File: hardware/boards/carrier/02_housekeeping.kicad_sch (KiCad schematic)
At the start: 11 parts, among them SW1 SKSCLCE010, U1 STM32G031G6U6

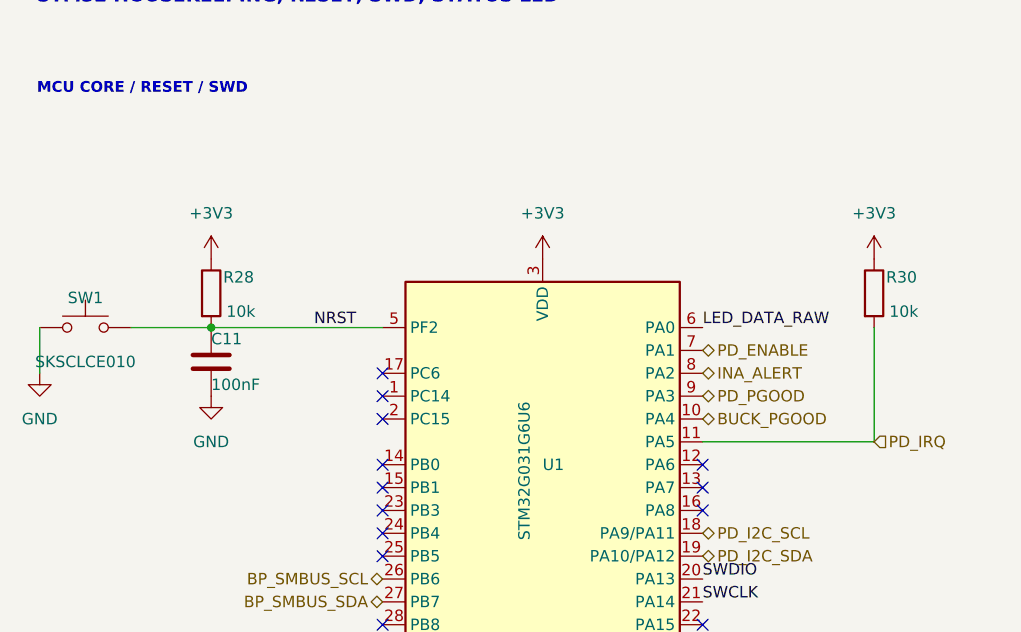
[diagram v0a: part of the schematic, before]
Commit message: hardware: move carrier button to GPIO
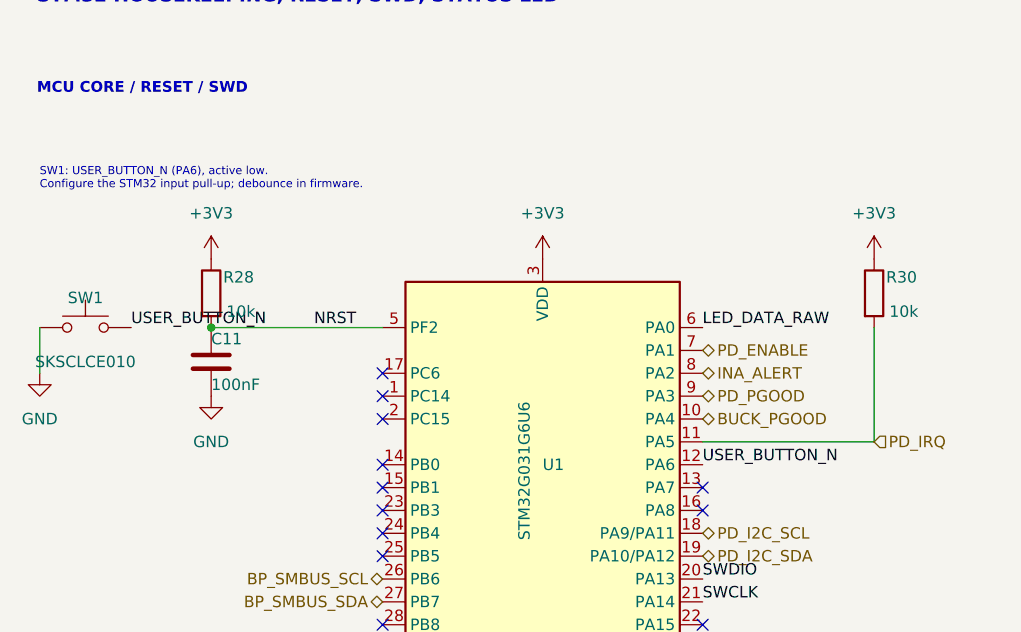
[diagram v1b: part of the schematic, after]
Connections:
- net NRST: no longer SW1.2
- net USER_BUTTON_N: now reaches U1.12 (PA6)
- net USER_BUTTON_N: now also SW1.2
- no-connect marks 14 -> 13
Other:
- note added: "SW1: USER_BUTTON_N (PA6), active low. Configure the STM32 input pull-up; debounce in firmware."
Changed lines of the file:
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@@
+		)
+	)
+	(text "SW1: USER_BUTTON_N (PA6), active low.\nConfigure the STM32 input pull-up; debounce in firmware."
+		(exclude_from_sim no)
+		(at 20.32 35.56 0)
+		(effects
+			(font
+				(size 0.9 0.9)
+			)
+			(justify left bottom)
 		)
 	)
@@
 		)
 	)
-	(wire
-		(pts
-			(xy 30.48 50.8) (xy 39.37 50.8)
-		)
-		(stroke
-			(width 0)
-			(type default)
-		)
-	)
 	(no_connect
 		(at 58.42 58.42)
-	)
-	(no_connect
-		(at 93.98 66.04)
 	)
 	(no_connect
@@
 		)
 	)
+	(label "USER_BUTTON_N"
+		(at 30.48 50.8 0)
+		(effects
+			(font
+				(size 1.27 1.27)
+			)
+			(justify left bottom)
+		)
+	)
+	(label "USER_BUTTON_N"
+		(at 93.98 66.04 0)
+		(effects
+			(font
+				(size 1.27 1.27)
+			)
+			(justify left bottom)
+		)
+	)

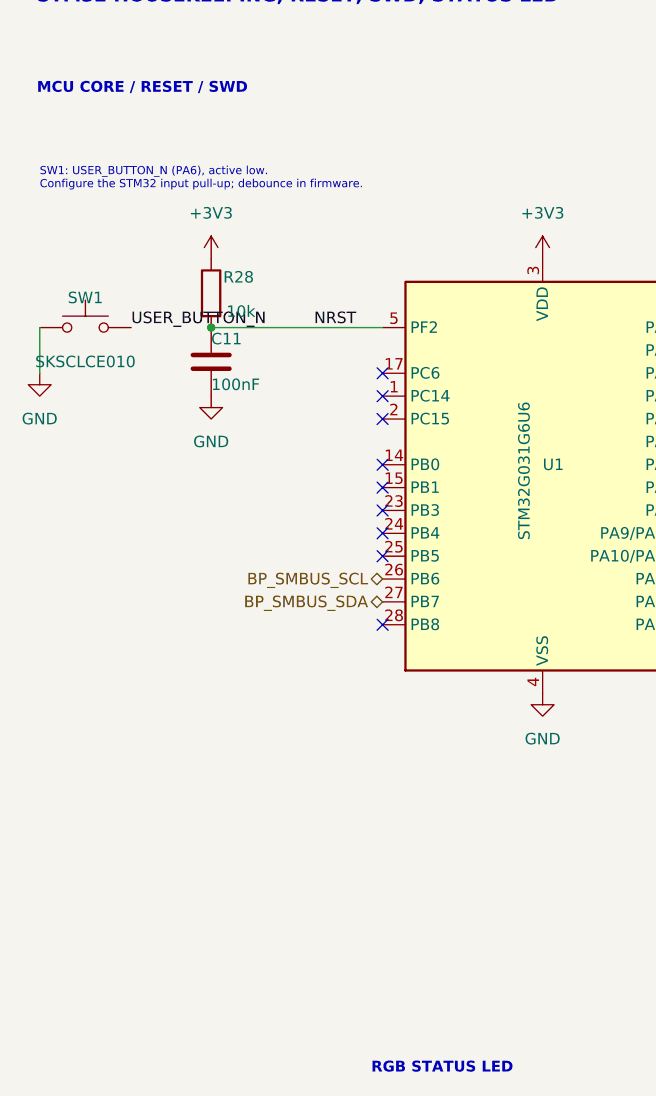
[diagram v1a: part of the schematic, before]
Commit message: hardware: add button debounce and ground stitching via
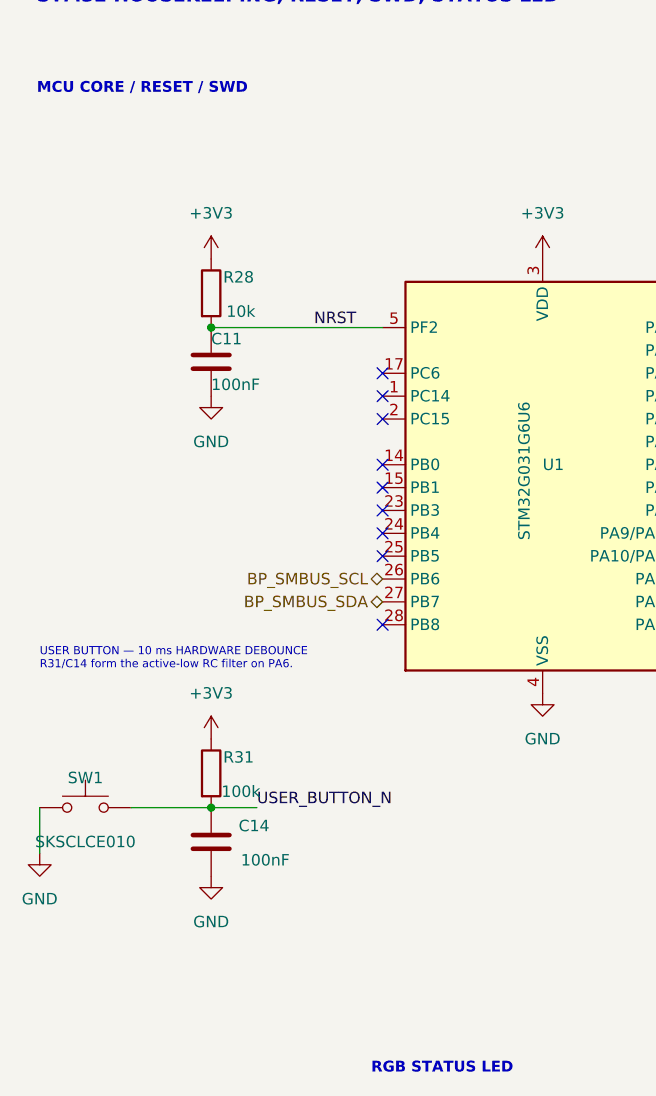
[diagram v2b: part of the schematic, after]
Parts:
- added C14: 100nF, Capacitor_SMD:C_0603_1608Metric, symbol Device:C
- added R31: 100k, Resistor_SMD:R_0603_1608Metric, symbol Device:R
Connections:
- net +3V3: now also R31.1
- net GND: now also C14.2
- net USER_BUTTON_N: now also C14.1, R31.2
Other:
- note added: "USER BUTTON — 10 ms HARDWARE DEBOUNCE R31/C14 form the active-low RC filter on PA6."
- note removed: "SW1: USER_BUTTON_N (PA6), active low. Configure the STM32 input pull-up; debounce in firmware."
- moved on the sheet: SW1

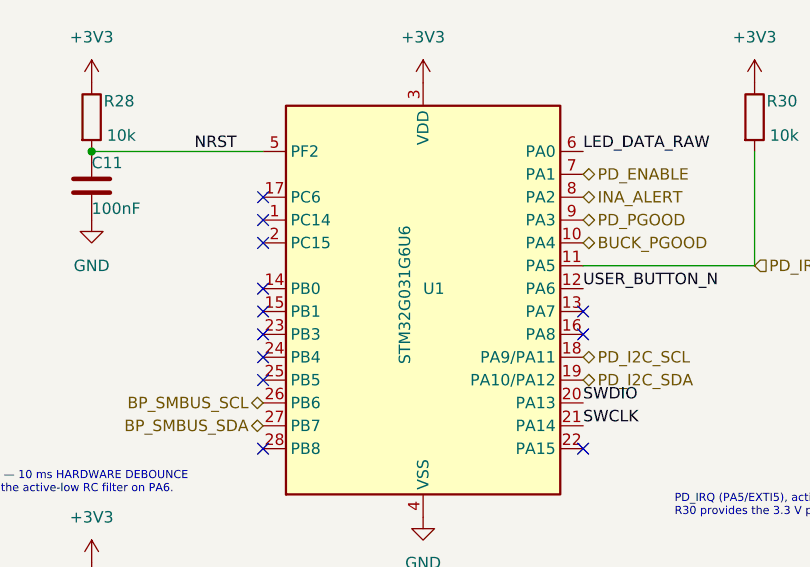
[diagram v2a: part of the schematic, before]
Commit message: Replace carrier MCU with STM32C092GCU7
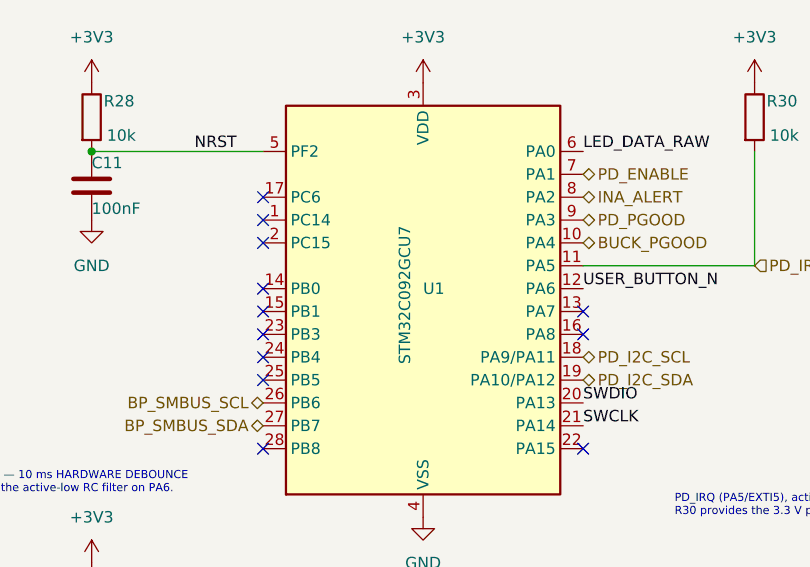
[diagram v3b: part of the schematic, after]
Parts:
- U1: value STM32G031G6U6 -> STM32C092GCU7; symbol MCU_ST_STM32G0:STM32G031G6Ux -> mini-rack-power:STM32C092GCUx; LCSC C432210 -> (none); MPN STM32G031G6U6 -> STM32C092GCU7
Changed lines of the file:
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@@
 	)
 	(symbol
-		(lib_id "MCU_ST_STM32G0:STM32G031G6Ux")
+		(lib_id "mini-rack-power:STM32C092GCUx")
 		(at 76.2 68.58 0)
 		(unit 1)
@@
 			)
 		)
-		(property "Value" "STM32G031G6U6"
+		(property "Value" "STM32C092GCU7"
 			(at 74.168 74.422 90)
 			(show_name no)
@@
 			)
 		)
-		(property "Datasheet" "https://www.st.com/resource/en/datasheet/stm32g031g6.pdf"
+		(property "Datasheet" "https://www.st.com/resource/en/datasheet/stm32c092gc.pdf"
 			(at 76.2 68.58 0)
 			(hide yes)
@@
 			)
 		)
-		(property "Description" "STMicroelectronics Arm Cortex-M0+ MCU, 32KB flash, 8KB RAM, 64 MHz, 1.7-3.6V, 26 GPIO, UFQFPN28"
+		(property "Description" "STMicroelectronics Arm Cortex-M0+ MCU, 256KB flash, 30KB RAM, 48 MHz, 2.0-3.6V, FDCAN, 26 GPIO, UFQFPN28"
 			(at 76.2 68.58 0)
 			(hide yes)
@@
 			)
 		)
-		(property "MPN" "STM32G031G6U6"
+		(property "MPN" "STM32C092GCU7"
 			(at 76.2 68.58 0)
 			(hide yes)
@@
 			)
 		)
-		(property "LCSC" "C432210"
+		(property "LCSC" ""
 			(at 76.2 68.58 0)
 			(hide yes)

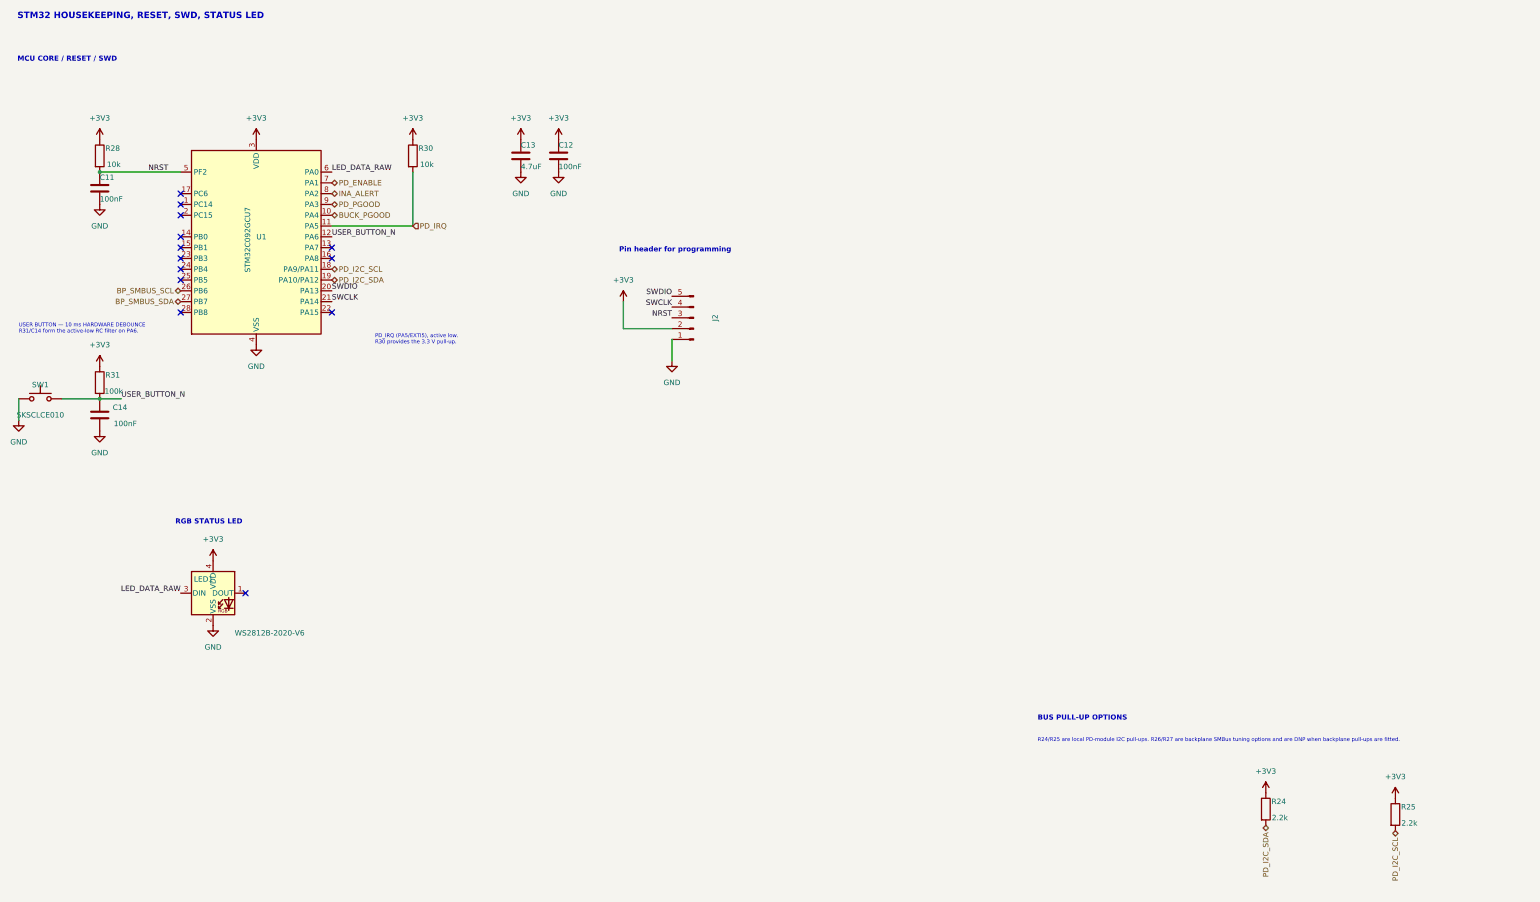
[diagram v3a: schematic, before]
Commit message: Replace carrier backplane SMBus with CAN-FD
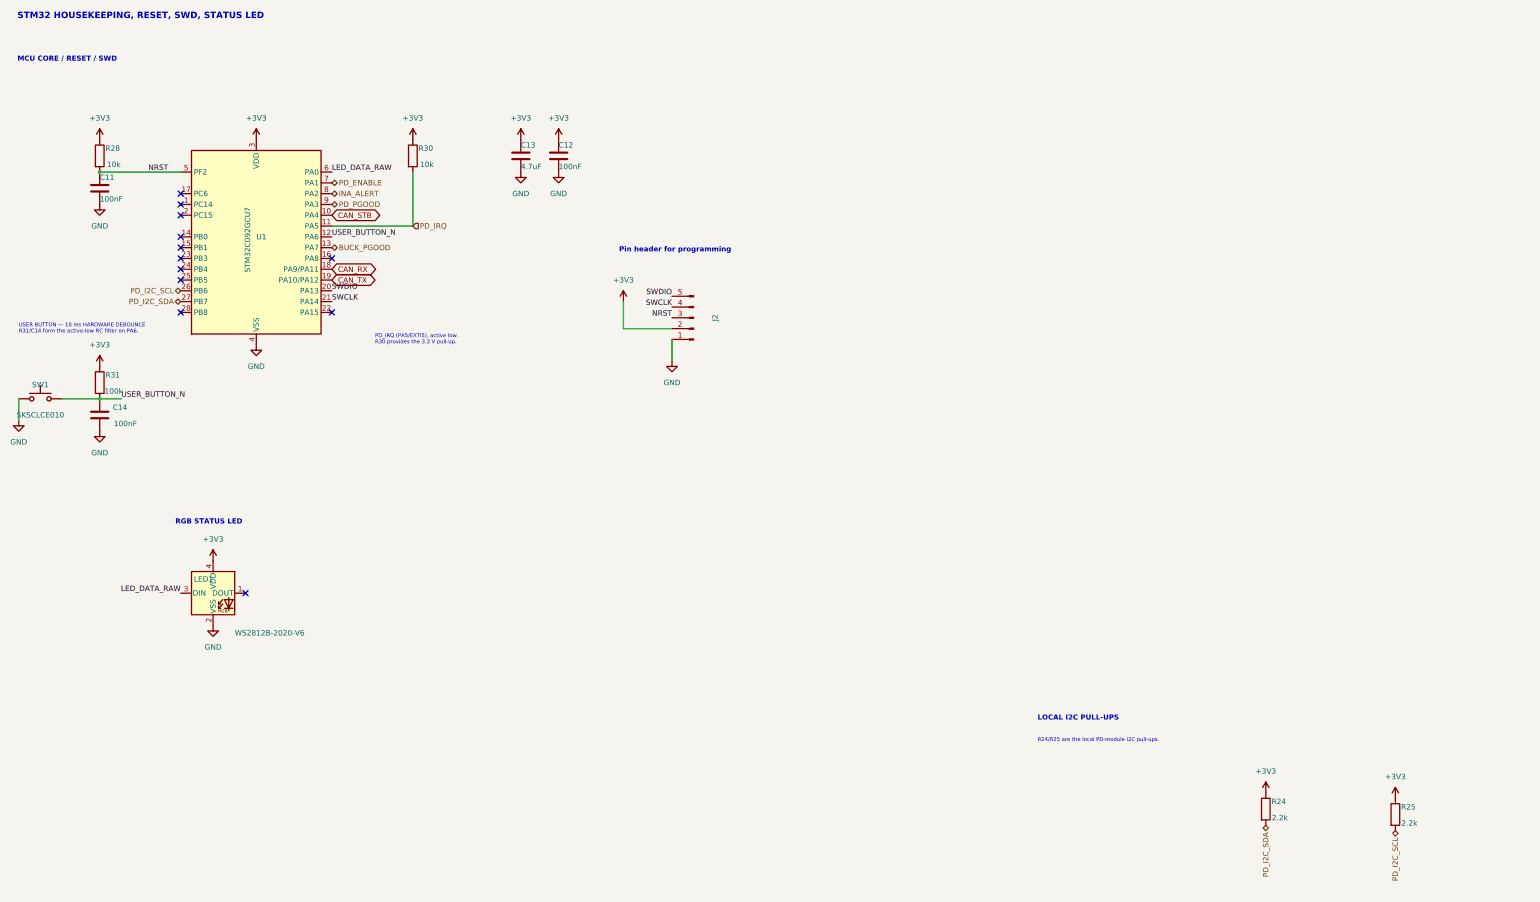
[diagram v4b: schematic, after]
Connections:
- net BP_SMBUS_SCL is gone; now on net PD_I2C_SCL: U1.26 (PB6)
- net BP_SMBUS_SDA is gone; now on net PD_I2C_SDA: U1.27 (PB7)
- net BUCK_PGOOD: now also U1.13 (PA7); no longer U1.10 (PA4)
- net PD_I2C_SCL: no longer U1.18 (PA9/PA11)
- net PD_I2C_SDA: no longer U1.19 (PA10/PA12)
- new net CAN_RX: U1.18 (PA9/PA11)
- new net CAN_STB: U1.10 (PA4)
- new net CAN_TX: U1.19 (PA10/PA12)
- no-connect marks 13 -> 12
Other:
- note added: "LOCAL I2C PULL-UPS"
- note added: "R24/R25 are the local PD-module I2C pull-ups."
- note removed: "BUS PULL-UP OPTIONS"
- note removed: "R24/R25 are local PD-module I2C pull-ups. R26/R27 are backplane SMBus tuning options and are DNP when backplane pull-ups are fitted."

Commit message: Move carrier LED data to PA8
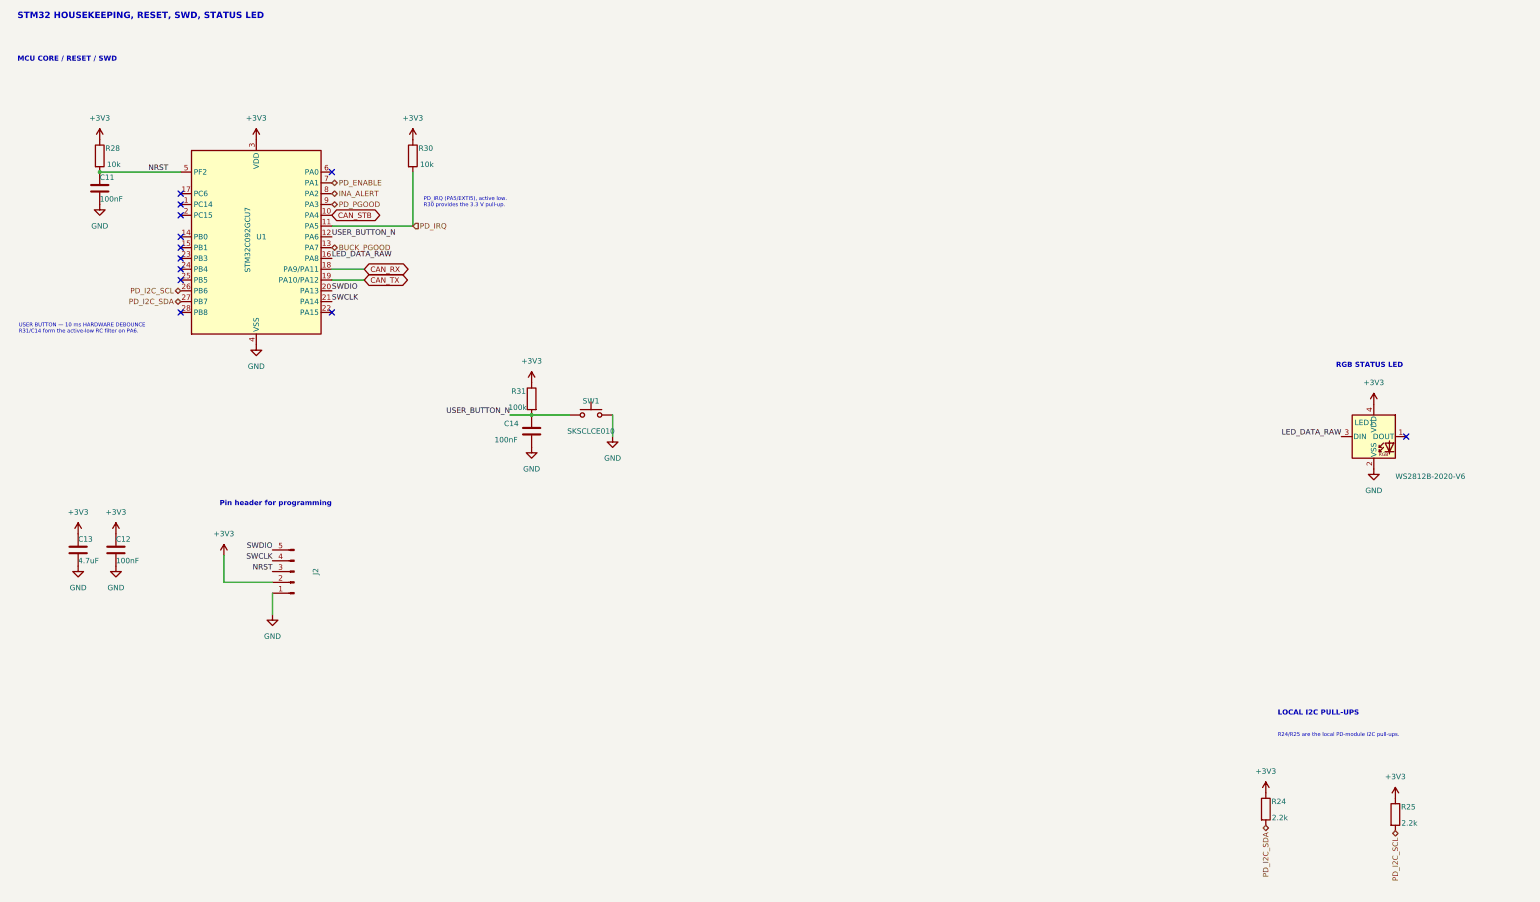
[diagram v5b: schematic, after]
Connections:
- net LED_DATA_RAW: now also U1.16 (PA8); no longer U1.6 (PA0)
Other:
- moved on the sheet: C12, C13, C14, J2, LED1, R31, SW1

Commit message: Move carrier PD enable to PC14
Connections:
- net PD_ENABLE: now also U1.1 (PC14); no longer U1.7 (PA1)
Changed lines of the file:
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@@
 	)
 	(no_connect
-		(at 58.42 58.42)
+		(at 93.98 53.34)
 	)
 	(no_connect
@@
 	(hierarchical_label "PD_ENABLE"
 		(shape bidirectional)
-		(at 93.98 53.34 0)
-		(effects
-			(font
-				(size 1.27 1.27)
-			)
-			(justify left bottom)
-		)
-	)
+		(at 58.42 58.42 180)
+		(effects
+			(font
+				(size 1.27 1.27)
+			)
+			(justify right bottom)
+		)
+	)
